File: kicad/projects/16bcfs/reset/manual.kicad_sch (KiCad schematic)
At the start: 1 part, among them SW1 SW_Push

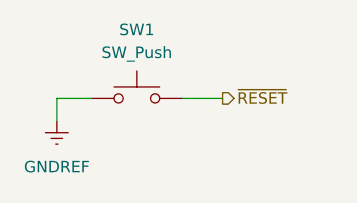
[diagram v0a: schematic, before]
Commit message: Added some debugging code
This is still not working.  I will need to revamp the reset routines for
the emulator to get this to work properly.  Everything will need an
initial state on construction and a `reset()` routine to place
everything into a proper state.  This in itself will be a major change.
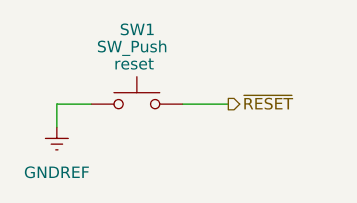
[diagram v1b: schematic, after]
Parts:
- SW1: name (none) -> reset
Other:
- moved on the sheet: SW1
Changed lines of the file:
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@@
     (comment 1 "Adam Clark (@eryjus)")
   )
-  (wire (pts (xy 132.08 94.615) (xy 132.08 97.155))
+  (wire (pts (xy 132.08 95.25) (xy 132.08 97.79))
     (stroke (width 0) (type default))
   )
-  (wire (pts (xy 146.05 94.615) (xy 150.495 94.615))
+  (wire (pts (xy 146.05 95.25) (xy 151.13 95.25))
     (stroke (width 0) (type default))
   )
-  (wire (pts (xy 135.89 94.615) (xy 132.08 94.615))
+  (wire (pts (xy 135.89 95.25) (xy 132.08 95.25))
     (stroke (width 0) (type default))
   )
-  (hierarchical_label "~{RESET}" (shape output) (at 150.495 94.615 0) (fields_autoplaced)
+  (hierarchical_label "~{RESET}" (shape output) (at 151.13 95.25 0) (fields_autoplaced)
     (effects (font (size 1.27 1.27)) (justify left))
   )
-  (symbol (lib_id "power:GNDREF") (at 132.08 97.155 0) (unit 1)
+  (symbol (lib_id "power:GNDREF") (at 132.08 97.79 0) (unit 1)
     (in_bom yes) (on_board yes) (dnp no) (fields_autoplaced)
-    (property "Reference" "#PWR03" (at 132.08 103.505 0)
+    (property "Reference" "#PWR016" (at 132.08 104.14 0)
       (effects (font (size 1.27 1.27)) hide)
     )
-    (property "Value" "GNDREF" (at 132.08 102.235 0)
+    (property "Value" "GNDREF" (at 132.08 102.87 0)
       (effects (font (size 1.27 1.27)))
     )
-    (property "Footprint" "" (at 132.08 97.155 0)
+    (property "Footprint" "" (at 132.08 97.79 0)
       (effects (font (size 1.27 1.27)) hide)
     )
-    (property "Datasheet" "" (at 132.08 97.155 0)
+    (property "Datasheet" "" (at 132.08 97.79 0)
       (effects (font (size 1.27 1.27)) hide)
     )
@@
       (project "reset"
         (path "/d0ae44e5-d74e-4df6-bf3d-e0535c5a7785/453050da-f061-41ea-8de6-e62b64039098"
-          (reference "#PWR03") (unit 1)
+          (reference "#PWR016") (unit 1)
         )
       )
     )
   )
-  (symbol (lib_id "Switch:SW_Push") (at 140.97 94.615 0) (unit 1)
-    (in_bom yes) (on_board yes) (dnp no) (fields_autoplaced)
-    (property "Reference" "SW1" (at 140.97 86.995 0)
-      (effects (font (size 1.27 1.27)))
+  (symbol (lib_id "Switch:SW_Push") (at 140.97 95.25 0) (unit 1)
+    (in_bom yes) (on_board yes) (dnp no)
+    (property "Reference" "SW1" (at 139.065 86.995 0)
+      (effects (font (size 1.27 1.27)) (justify left))
     )
-    (property "Value" "SW_Push" (at 140.97 89.535 0)
-      (effects (font (size 1.27 1.27)))
+    (property "Value" "SW_Push" (at 136.525 88.9 0)
+      (effects (font (size 1.27 1.27)) (justify left))
     )
-    (property "Footprint" "" (at 140.97 89.535 0)
+    (property "Footprint" "" (at 140.97 90.17 0)
       (effects (font (size 1.27 1.27)) hide)
     )
-    (property "Datasheet" "~" (at 140.97 89.535 0)
+    (property "Datasheet" "~" (at 140.97 90.17 0)
       (effects (font (size 1.27 1.27)) hide)
     )
+    (property "name" "reset" (at 138.43 90.805 0)
+      (effects (font (size 1.27 1.27)) (justify left))
+    )
     (pin "2")
